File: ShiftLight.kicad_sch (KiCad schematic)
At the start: 20 parts, among them U1 MSPM0C1104SDDFR, U2 LMR544xx, U3 KTD2052A/B

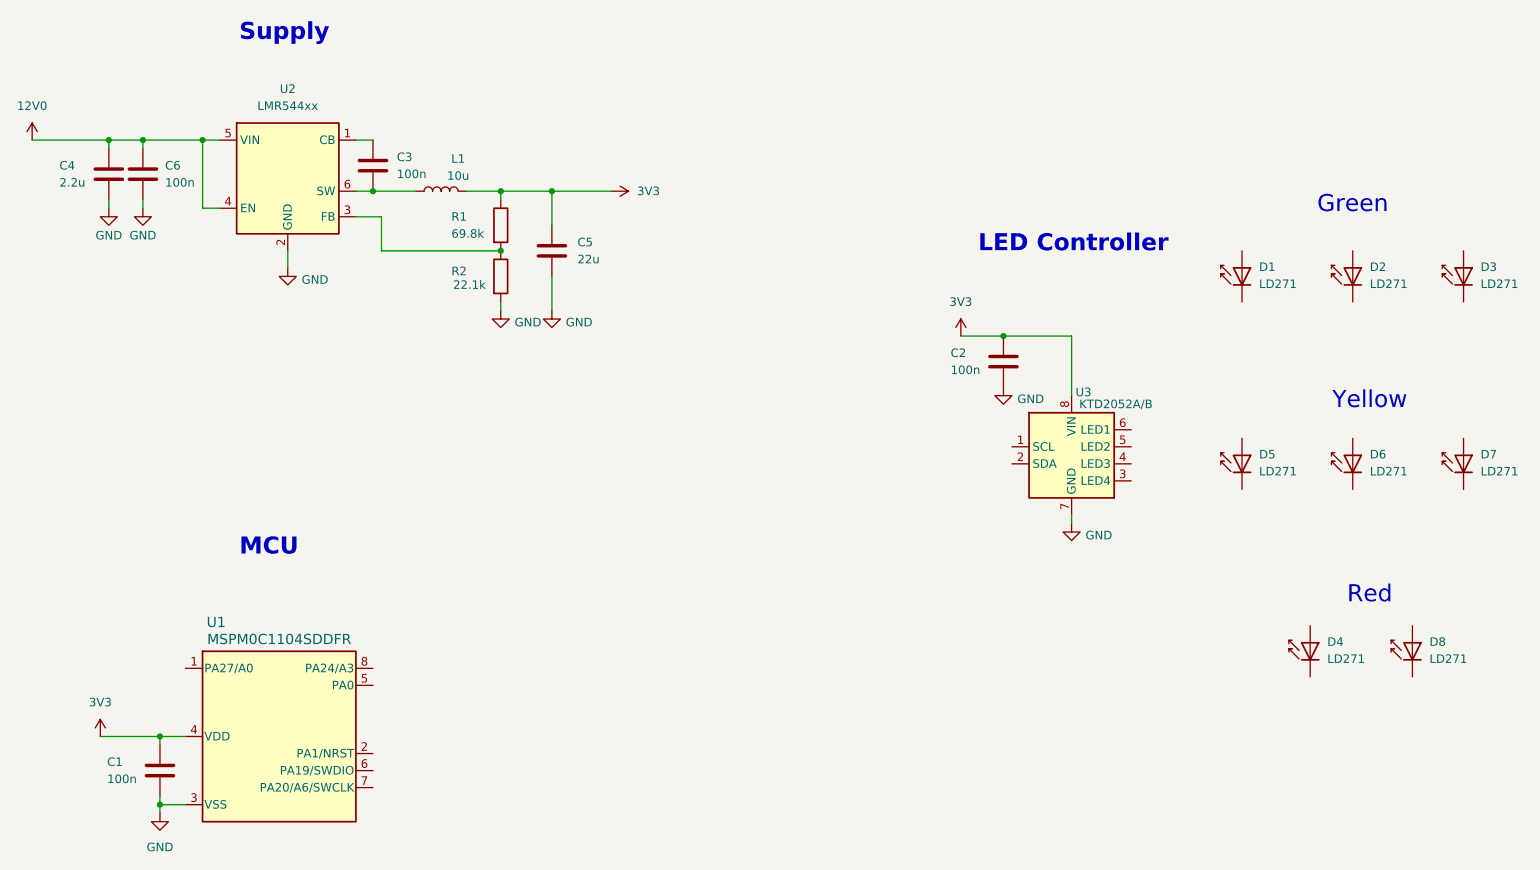
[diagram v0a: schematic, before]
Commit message: Update schematic, make hierarchical
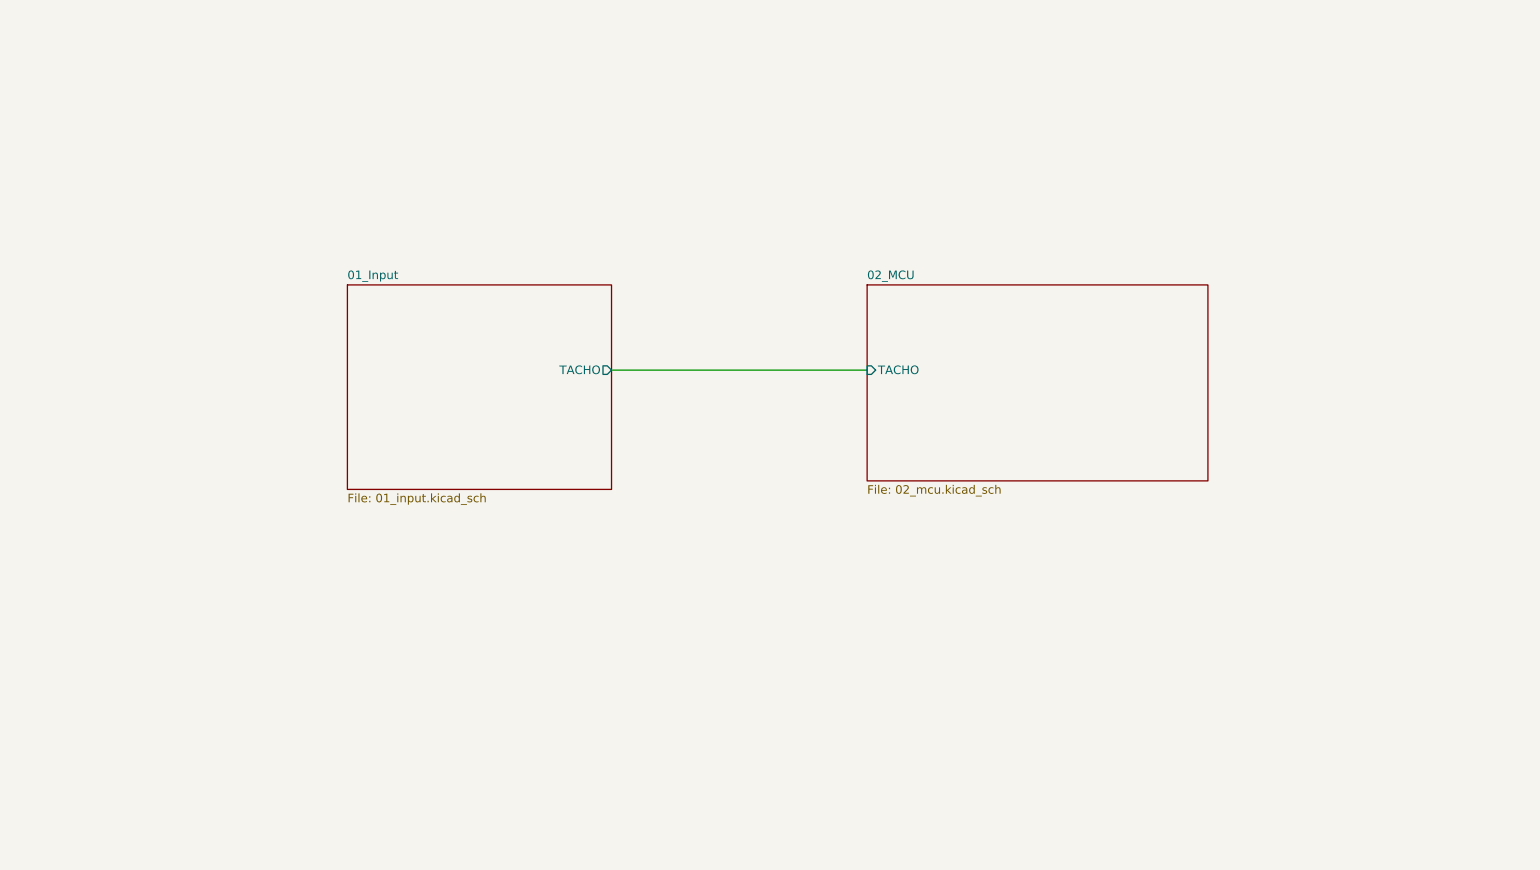
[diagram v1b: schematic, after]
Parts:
- removed C1, C2, C3, C6: 100n, Capacitor_SMD:C_0603_1608Metric, symbol Device:C
- removed C4: 2.2u, symbol Device:C
- removed C5: 22u, symbol Device:C
- removed D1, D2, D3, D4, D5, D6, D7, D8: LD271, LED_THT:LED_D5.0mm_IRGrey, symbol LED:LD271
- removed L1: 10u, symbol Device:L
- removed R1: 69.8k, Resistor_SMD:R_0603_1608Metric, symbol Device:R
- removed R2: 22.1k, Resistor_SMD:R_0603_1608Metric, symbol Device:R
- removed U1: MSPM0C1104SDDFR, Package_TO_SOT_SMD:SOT-23-8, symbol Personal_lib:MSPM0C1104SDDFR
- removed U2: LMR544xx, Package_TO_SOT_SMD:SOT-23-6, symbol Personal_lib:LMR544xx
- removed U3: KTD2052A/B, Package_DFN_QFN:DFN-8-1EP_2x2mm_P0.5mm_EP0.9x1.5mm, symbol Personal_lib:KTD2052A/B
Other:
- added sheet 01_Input (01_input.kicad_sch)
- added sheet 02_MCU (02_mcu.kicad_sch)
- note removed: "Green"
- note removed: "LED Controller"
- note removed: "MCU"
- note removed: "Red"
- note removed: "Supply"
- note removed: "Yellow"

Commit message: Ci: Fill title header in generated schematic
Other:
- title: (none) -> ${PROJECTNAME}
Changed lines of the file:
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@@
 	(generator_version "8.0")
 	(paper "A4")
+	(title_block
+		(title "${PROJECTNAME}")
+		(date "${ISSUE_DATE}")
+		(rev "${REVISION}")
+	)
 	(wire
 		(pts
